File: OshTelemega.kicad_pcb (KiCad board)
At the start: 4 copper layers, 30 x 80 mm, 139 parts, among them J1 USB_C_Receptacle_USB2.0_16P, J10 SERVOS, J12 DEBUG, J2 Conn_02x04_Counter_Clockwise, J3 SMA_Edgelaunch, J4 USB_C_Receptacle_USB2.0_16P, J5 UFL, J6 RIGHT, J7 LEFT, J8 Conn_01x02, U1 STM32L151VCTx, U10 MMC5983MA, U11 TSM200N03, U12 LM293QT, U13 LM293QT, U14 TSM200N03, U15 LM293QT, U16 TSM200N03, U17 MCP73831-2-OT, U18 TC2185-3.3VxCTTR, U2 WE-TVS-82400102, U3 ADXL375, U4 MS5607-02BA, U5 MAX-M10S, U6 MCP130-xxxxTT, U7 W25Q64JVXGIQ, U8 CC1200, U9 BMI088, Y1 ABM8W-40.0000MHZ

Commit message: v0.1 done. Redesigning for potential mosaic integration
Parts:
- removed BZ1: Buzzer, Buzzer_Beeper:Buzzer_TDK_PS1240P02BT_D12.2mm_H6.5mm
- removed J1: USB_C_Receptacle_USB2.0_16P, Connector_USB:USB_C_Receptacle_GCT_USB4105-xx-A_16P_TopMnt_Horizontal
- removed U7: W25Q64JVXGIQ, FCU2025Lib:DFN_XGIQ TR_WIN
- added H5: MountingHole_Pad, MountingHole:MountingHole_3.2mm_M3_DIN965_Pad, F.Cu at (47.0, 65.5)
- added U19: W25Q64JVXGIQ, FCU2025Lib:DFN_XGIQ TR_WIN, B.Cu at (39.8, 39.9)
- moved J4 99.3 mm to (38.7, 96.7)
- moved R35 68.8 mm to (21.2, 80.1), turned to 90 degrees
- moved J10 68.7 mm to (36.4, 67.0), turned to 90 degrees
- moved R36 66.7 mm to (21.2, 78.2), turned to -90 degrees
- moved U16 65.7 mm to (23.5, 79.0), turned to -90 degrees
- moved R31 65.3 mm to (25.8, 80.1), turned to 90 degrees
- moved R33 64.2 mm to (21.2, 76.0), turned to 90 degrees
- moved R34 63.4 mm to (22.2, 76.0), turned to -90 degrees
- moved R32 63.0 mm to (25.8, 78.2), turned to -90 degrees
- moved R29 62.0 mm to (23.8, 76.0), turned to 90 degrees
- moved R30 61.2 mm to (24.8, 76.0), turned to -90 degrees
- moved U15 60.0 mm to (23.2, 73.8), turned to 0 degrees
- moved J2 53.9 mm to (30.3, 67.0), turned to 90 degrees
- moved R23 53.3 mm to (36.0, 76.6), turned to -90 degrees
- moved R24 51.6 mm to (36.0, 78.5), turned to 90 degrees
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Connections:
- J12 pad 2: /NRST -> /SWCLK
- J12 pad 4: /SWCLK -> /NRST
- J2 pad 3: /MOSI2 -> V_LIPO
- J2 pad 5: /CS_COMP1 -> /MOSI2
- J2 pad 6: /CS_COMP0 -> /CS_COMP1
- J2 pad 8: V_LIPO -> /CS_COMP0
- J4 pad A1: Net-(J4-GND-PadA1) -> GND
- J4 pad A12: Net-(J4-GND-PadA1) -> GND
- J4 pad A4: Net-(J4-VBUS-PadA4) -> VBUS
- J4 pad A5: unconnected-(J4-CC1-PadA5) -> Net-(J4-CC1)
- J4 pad A6: unconnected-(J4-D+-PadA6) -> Net-(J4-D+-PadA6)
- J4 pad A7: unconnected-(J4-D--PadA7) -> Net-(J4-D--PadA7)
- J4 pad A9: Net-(J4-VBUS-PadA4) -> VBUS
- J4 pad B1: Net-(J4-GND-PadA1) -> GND
- J4 pad B12: Net-(J4-GND-PadA1) -> GND
- J4 pad B4: Net-(J4-VBUS-PadA4) -> VBUS
- J4 pad B5: unconnected-(J4-CC2-PadB5) -> Net-(J4-CC2)
- J4 pad B6: unconnected-(J4-D+-PadB6) -> Net-(J4-D+-PadA6)
- J4 pad B7: unconnected-(J4-D--PadB7) -> Net-(J4-D--PadA7)
- J4 pad B9: Net-(J4-VBUS-PadA4) -> VBUS
- J4 pad S1: unconnected-(J4-SHIELD-PadS1) -> GND
- R1 pad 1: Net-(J1-CC1) -> Net-(J4-CC1)
- R10 pad 1: Net-(J1-D+-PadA6) -> Net-(J4-D+-PadA6)
- R2 pad 1: Net-(J1-CC2) -> Net-(J4-CC2)
- R21 pad 2: /FIRE_C -> /FIRE_D
- R22 pad 1: /FIRE_C -> /FIRE_D
- R22 pad 2: /GATE_C -> /GATE_D
- R23 pad 1: /FET_C -> /FET_D
- R23 pad 2: /SENSE_C -> /SENSE_D
- R24 pad 2: /SENSE_C -> /SENSE_D
- R25 pad 2: /FIRE_D -> /FIRE_C
- R26 pad 1: /FIRE_D -> /FIRE_C
- R26 pad 2: /GATE_D -> /GATE_C
- R27 pad 1: /FET_D -> /FET_C
- R27 pad 2: /SENSE_D -> /SENSE_C
- R28 pad 2: /SENSE_D -> /SENSE_C
- R6 pad 2: Net-(J10-Pin_3) -> Net-(J10-Pin_4)
- R7 pad 2: Net-(J10-Pin_4) -> Net-(J10-Pin_3)
- R9 pad 1: Net-(J1-D--PadA7) -> Net-(J4-D--PadA7)
- U14 pad 2: /GATE_D -> /GATE_C
- U14 pad 4: /GATE_C -> /GATE_D
- U14 pad 5_6: /FET_C -> /FET_D
- U14 pad 7_8: /FET_D -> /FET_C
- U15 pad 1: /GATE_E -> /GATE_F
- U15 pad 7: /GATE_F -> /GATE_E
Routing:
- net GND: track 58.8 -> 123.1 mm, vias 51 -> 109
- net /CMP_LDO_IN: track 5.13 -> 66.8 mm, vias 0 -> 5
- net V_LIPO: track 4.18 -> 61.6 mm
- net /SENSE_A: track 0.89 -> 57.1 mm, vias 0 -> 2
- net /CMP_RAIL: track 10.7 -> 66.9 mm, vias 2 -> 6
- net /SENSE_B: track 0.88 -> 56.5 mm, vias 0 -> 2
- net /V_PBATT: track 1.00 -> 52.4 mm, vias 0 -> 2
- net /V_BATT: track 1.00 -> 49.6 mm, vias 0 -> 2
- net /SENSE_F: track 0.87 -> 48.3 mm, vias 0 -> 4
- net /MISO2: track 9.17 -> 53.6 mm, vias 0 -> 2
- net /FIRE_B: track 1.00 -> 41.9 mm, vias 0 -> 2
- net /SENSE_C: track 0.89 -> 41.2 mm, vias 0 -> 6
- net /SCK2: track 4.25 -> 44.2 mm, vias 0 -> 2
- net /SENSE_D: track 0.88 -> 40.7 mm, vias 0 -> 2
- net /SENSE_E: track 0.89 -> 39.6 mm, vias 0 -> 4
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- added copper zone on B.Cu, net /FET_C
- added copper zone on B.Cu, net /FET_D
- added copper zone on B.Cu, net /FET_E
- added copper zone on B.Cu, net /FET_F
- added copper zone on In1.Cu, net V_PYRO
- removed copper zone on B.Cu, net VBUS
- removed copper zone on F.Cu, net V_PYRO

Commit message: before adding 10 pin companion
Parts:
- removed J12: DEBUG, Connector_PinHeader_1.27mm:PinHeader_2x02_P1.27mm_Vertical
- added J1: Conn_ARM_SWD_TagConnect_TC2030-NL, Connector:Tag-Connect_TC2030-IDC-NL_2x03_P1.27mm_Vertical, F.Cu at (48.0, 58.6)
- moved L6 0.68 mm to (37.1, 28.9), turned to 90 degrees
- moved C41 0.64 mm to (36.2, 28.9), turned to -90 degrees
- moved L1 0.52 mm to (42.6, 29.4)
- moved L8 0.14 mm to (35.3, 26.9)
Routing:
- net /NRST: track 110.3 -> 101.0 mm, vias 6 -> 4
- net /SWDIO: track 13.2 -> 8.94 mm, vias 0 -> 3
- net /SWCLK: track 10.1 -> 11.9 mm, vias 1 -> 3
- net /AC_MOSI1: track 19.8 -> 18.3 mm
- net /AC_MISO1: track 19.3 -> 17.9 mm
- net /AC_SCK1: track 23.8 -> 22.6 mm
- net Net-(C40-Pad1): track 3.47 -> 2.53 mm
- net GND: track 123.1 -> 123.8 mm, vias 109 -> 113
- net Net-(J3-In): track 3.71 -> 4.28 mm
- net +3V3: track 79.5 -> 79.8 mm, vias 34 -> 35

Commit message: v0.2 done - just needs review and silkscreens
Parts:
- removed FL1: B39162B4300F210, Filter:Filter_1411-5_1.4x1.1mm
- added C43: 10nF X7R, Capacitor_SMD:C_0402_1005Metric, B.Cu at (34.1, 35.5)
- added C44: 0.1uF, Capacitor_SMD:C_0402_1005Metric, B.Cu at (48.9, 71.2)
- added D2: BAT54CW, Package_TO_SOT_SMD:SOT-323_SC-70, B.Cu at (46.9, 74.7)
- added D5: LED_Dual_AAKK, LED_SMD:LED_LiteOn_LTST-C19HE1WT, F.Cu at (27.3, 65.4)
- added FB2: LQG15HS47NJ02, Inductor_SMD:L_0402_1005Metric, B.Cu at (33.2, 33.6)
- added J9: Conn_02x05_Counter_Clockwise, Connector_PinHeader_1.27mm:PinHeader_2x05_P1.27mm_Vertical, F.Cu at (37.2, 66.2)
- added Q1: SiA449DJ, Package_TO_SOT_SMD:Vishay_PowerPAK_SC70-6L_Single, B.Cu at (31.5, 87.4)
- added Q2: AO3400A, Package_TO_SOT_SMD:SOT-23, B.Cu at (31.5, 81.7)
- added Q3: SiA449DJ, Package_TO_SOT_SMD:Vishay_PowerPAK_SC70-6L_Single, B.Cu at (32.0, 84.7)
- added R49: 100k, Resistor_SMD:R_0402_1005Metric, B.Cu at (29.8, 88.0)
- added R50: 1k, Resistor_SMD:R_0402_1005Metric, B.Cu at (26.1, 64.7)
- added R51: 1k, Resistor_SMD:R_0402_1005Metric, B.Cu at (45.1, 69.2)
- added R52: 100k, Resistor_SMD:R_0402_1005Metric, B.Cu at (48.6, 74.0)
- added R53: 100k, Resistor_SMD:R_0402_1005Metric, B.Cu at (30.2, 85.1)
- added R54: 10R 0.25W, Resistor_SMD:R_0402_1005Metric, B.Cu at (33.2, 35.5)
- added U21: SN74LVC1G80QDCKTQ1, Package_TO_SOT_SMD:SOT-353_SC-70-5, B.Cu at (47.0, 71.3)
- added U7: DRV5012AEDMRR, Package_SON:Texas_X2SON-4-1EP_1.1x1.4mm_P0.5mm_EP0.8x0.6mm, F.Cu at (24.1, 66.0)
- C21: footprint Inductor_SMD:L_0402_1005Metric -> Capacitor_SMD:C_0402_1005Metric
- FB1: value FerriteBead -> LI0402C221R-10
- J1: value Conn_ARM_SWD_TagConnect_TC2030-NL -> TAGCONNECT
- J2: value Conn_02x04_Counter_Clockwise -> Conn_01x02; footprint Connector_PinHeader_1.27mm:PinHeader_2x04_P1.27mm_Vertical -> Connector_PinHeader_1.27mm:PinHeader_1x02_P1.27mm_Vertical
- J8: value Conn_01x02 -> BATT
- moved U6 13.5 mm to (47.8, 41.0), turned to 180 degrees
- moved C10 13.4 mm to (48.1, 43.2), turned to 0 degrees
- moved D1 13.2 mm to (34.8, 85.5), turned to 90 degrees
- moved J2 12.3 mm to (21.4, 58.6), turned to 0 degrees
- moved J5 10.7 mm to (35.4, 38.9), turned to 0 degrees
- moved C21 7.23 mm to (27.7, 94.6), turned to 0 degrees
- moved J10 5.26 mm to (31.2, 66.2)
- moved U19 2.73 mm to (42.4, 40.5)
- moved R40 2.43 mm to (25.3, 90.2)
- moved C23 2.41 mm to (23.7, 92.5)
- moved C24 2.41 mm to (22.8, 86.2)
- moved R41 2.41 mm to (25.3, 88.3)
- moved R42 2.41 mm to (24.3, 89.4)
- moved R43 2.41 mm to (24.3, 87.5)
- moved U18 2.41 mm to (22.1, 89.2)
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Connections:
- C23 pad 2: Net-(D1-K) -> V_LIPO
- D1 pad 1: Net-(D1-K) -> V_LIPO
- D1 pad 2: V_LIPO -> /MGSW_OUT
- J2 pad 1: GND -> /BUZZ
- J2 pad 2: /SCK2 -> GND
- J7 pad 8: V_CHARGE -> V_PROT
- R40 pad 2: Net-(D1-K) -> V_LIPO
- U1 pad 68: unconnected-(U1-PA9-Pad68) -> /TX1
- U1 pad 69: unconnected-(U1-PA10-Pad69) -> /RX1
- U18 pad 1: Net-(D1-K) -> V_LIPO
- U18 pad 3: Net-(D1-K) -> V_LIPO
- U5 pad 11: Net-(U5-RF_IN) -> Net-(J5-In)
- U5 pad 14: unconnected-(U5-VCC_RF-Pad14) -> Net-(U5-VCC_RF)
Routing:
- net /MGSW_IN: track 0.00 -> 93.4 mm, vias 0 -> 3
- net /HALL_OUT: track 0.00 -> 50.1 mm, vias 0 -> 6
- net /TX1: track 0.00 -> 30.8 mm, vias 0 -> 4
- net Net-(Q2-G): track 0.00 -> 27.4 mm, vias 0 -> 4
- net Net-(D5-A2): track 0.00 -> 24.8 mm, vias 0 -> 5
- net /NRST: track 101.0 -> 81.7 mm
- net /RX1: track 0.00 -> 17.4 mm, vias 0 -> 2
- net Net-(D1-K): track 12.1 -> 0.00 mm
- net /CS_COMP1: track 6.40 -> 17.7 mm
- net /CS_COMP0: track 6.72 -> 17.7 mm
- net /MOSI2: track 49.7 -> 40.7 mm, vias 3 -> 2
- net /SCK2: track 44.2 -> 52.6 mm, vias 2 -> 4
- net /CS_MAG: track 13.5 -> 21.0 mm, vias 0 -> 4
- net /BUZZ: track 0.00 -> 7.47 mm, vias 0 -> 2
- net V_PROT: track 0.00 -> 6.56 mm
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
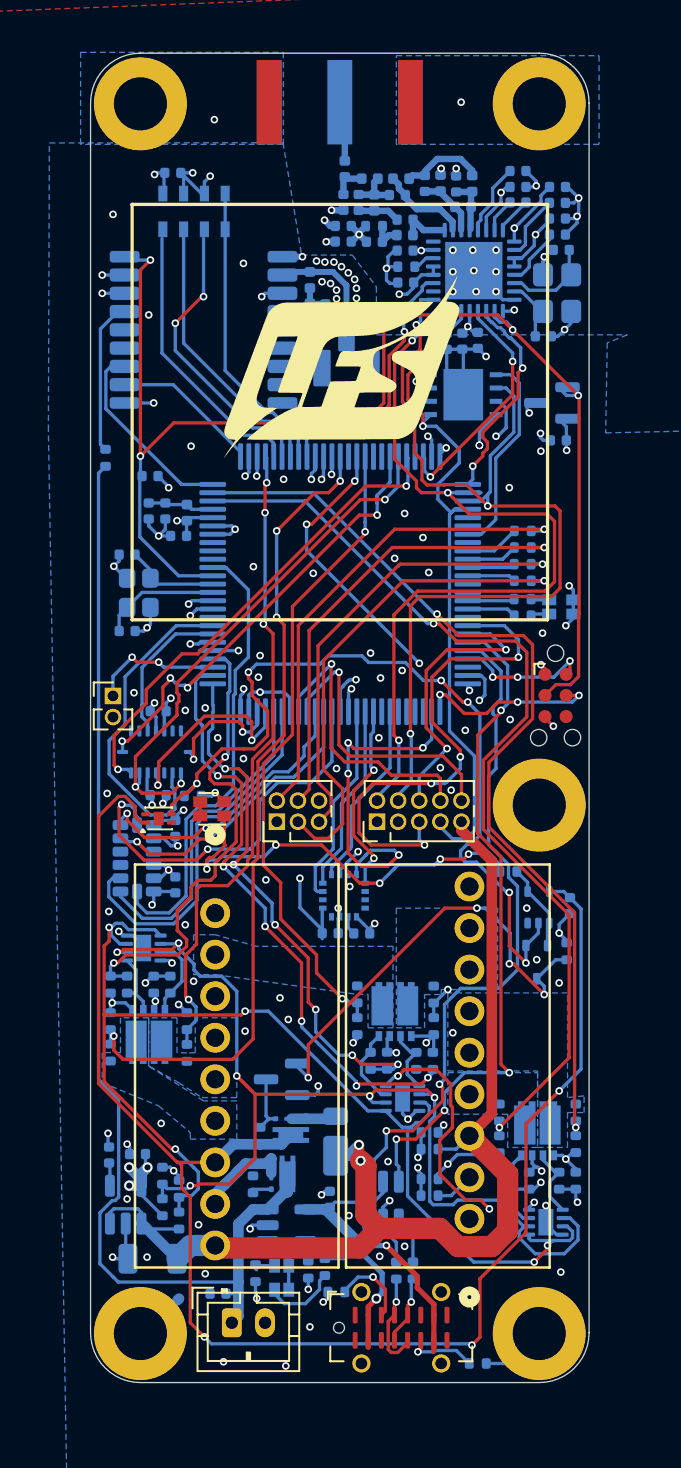
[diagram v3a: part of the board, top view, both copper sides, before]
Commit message: some jlc manufacturing considerations
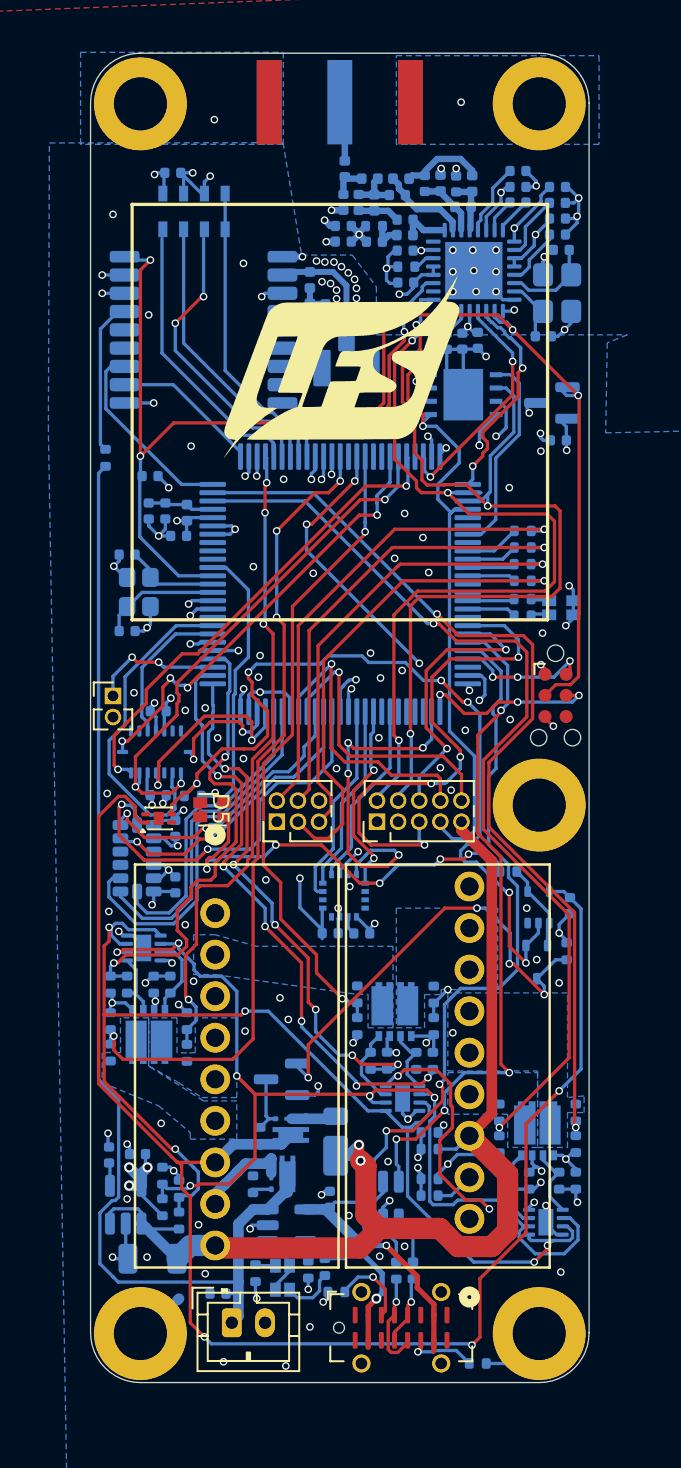
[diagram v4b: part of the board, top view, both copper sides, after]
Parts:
- removed ECS-160-8-36Q-AES-TR1: Crystal_GND24, Crystal:Crystal_SMD_2520-4Pin_2.5x2.0mm
- added X2: ECS-160-8-36Q-AES-TR, Crystal:Crystal_SMD_2520-4Pin_2.5x2.0mm, B.Cu at (22.9, 52.4)
- D3, D4, D5: footprint LED_SMD:LED_LiteOn_LTST-C19HE1WT -> FCU2025Lib:DualLED0606
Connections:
- D4 pad 3: Net-(D4-A2) -> Net-(D4-K1)
- D4 pad 4: Net-(D4-K2) -> Net-(D4-A1)
- R38 pad 2: Net-(D4-K2) -> Net-(D4-K1)
- R39 pad 1: Net-(D4-A1) -> Net-(D4-A2)
- U17 pad 1: Net-(D4-A2) -> Net-(D4-A1)
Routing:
- net Net-(D4-K1): track 0.00 -> 1.58 mm
- net Net-(D4-K2): track 1.17 -> 0.00 mm

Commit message: fixed wrong orientation on mag switch mosfet
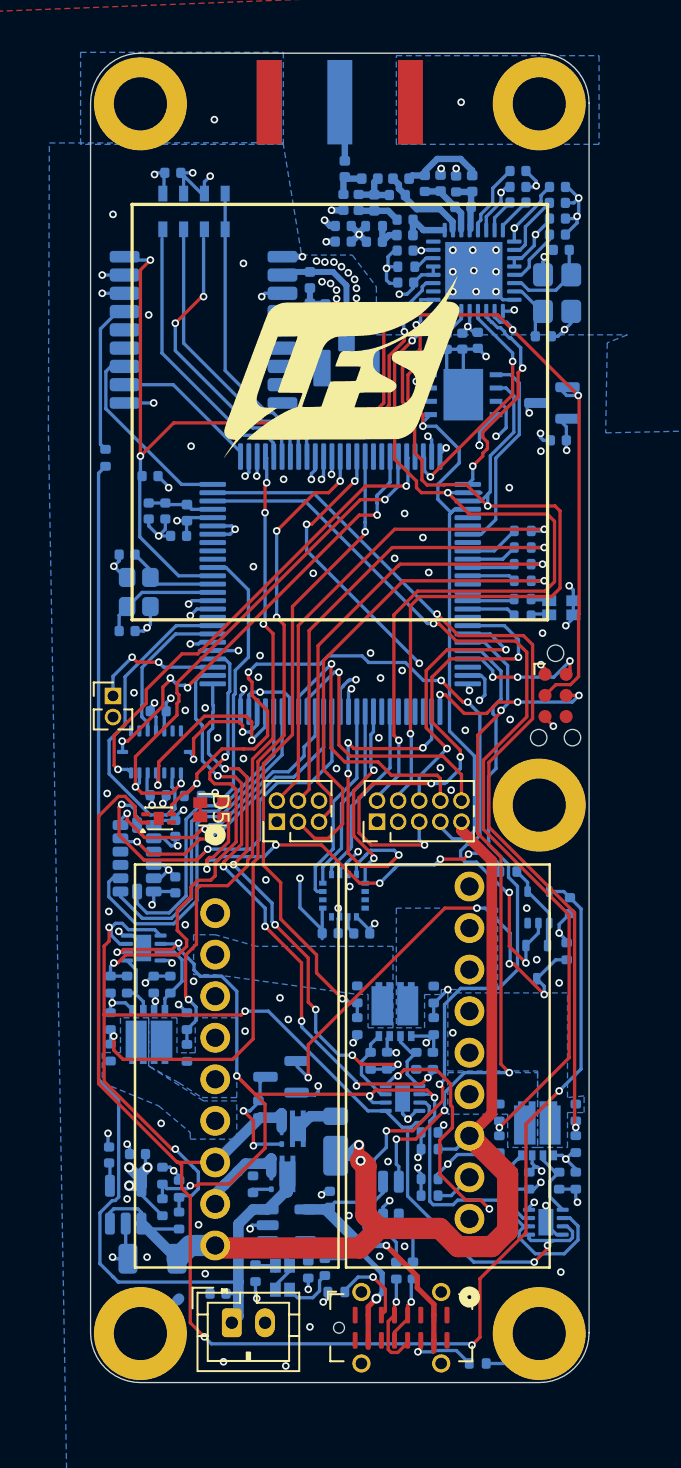
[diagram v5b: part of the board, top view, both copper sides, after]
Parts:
- X2: value ECS-160-8-36Q-AES-TR -> ECS-160-8-36Q-AES-TR1
- moved R53 1.60 mm to (30.1, 83.5)
- moved Q2 0.15 mm to (31.5, 81.5)
- moved Q3 0.11 mm to (32.1, 84.7), turned to 90 degrees
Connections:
- Q3 pad 1: /MGSW_IN -> /MGSW_OUT
- Q3 pad 4: /MGSW_OUT -> /MGSW_IN
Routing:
- net Net-(Q2-D): track 3.57 -> 6.92 mm, vias 0 -> 2
- net /MGSW_IN: track 93.4 -> 94.3 mm

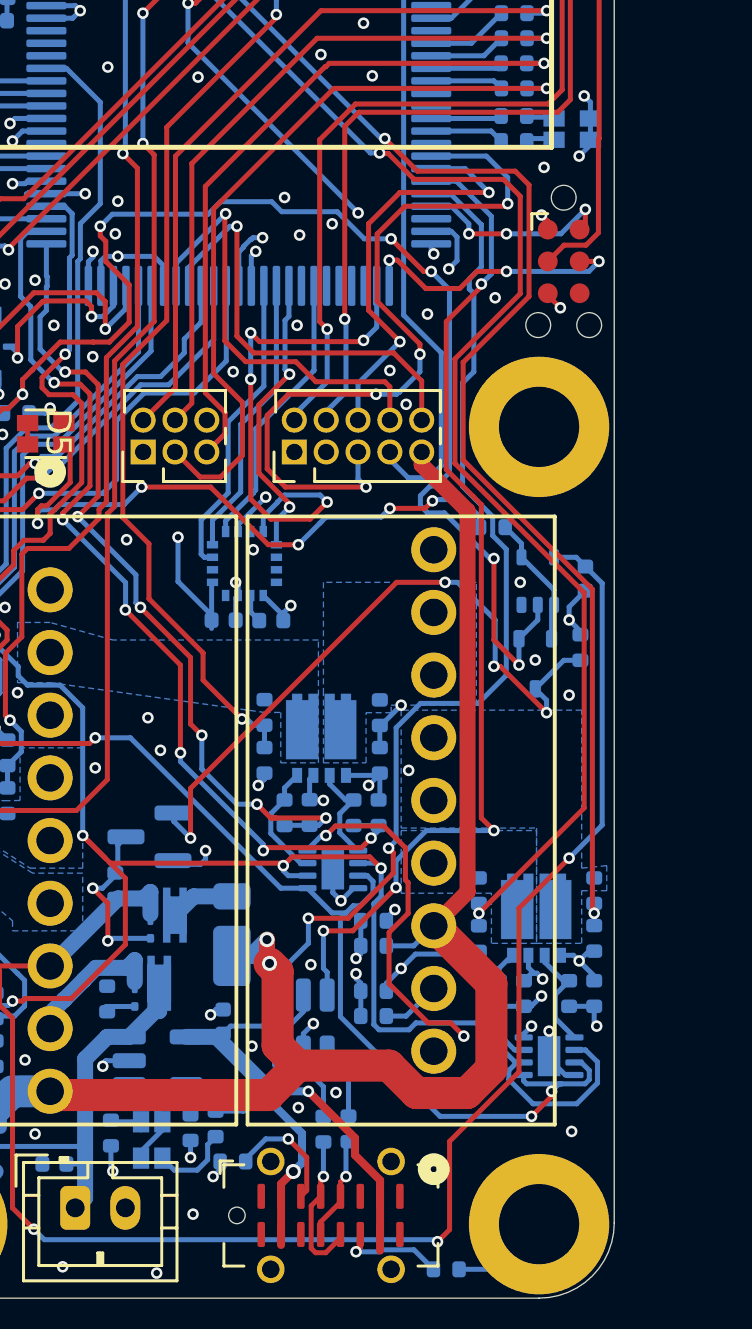
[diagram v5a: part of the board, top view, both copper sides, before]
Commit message: added pyro rp protection
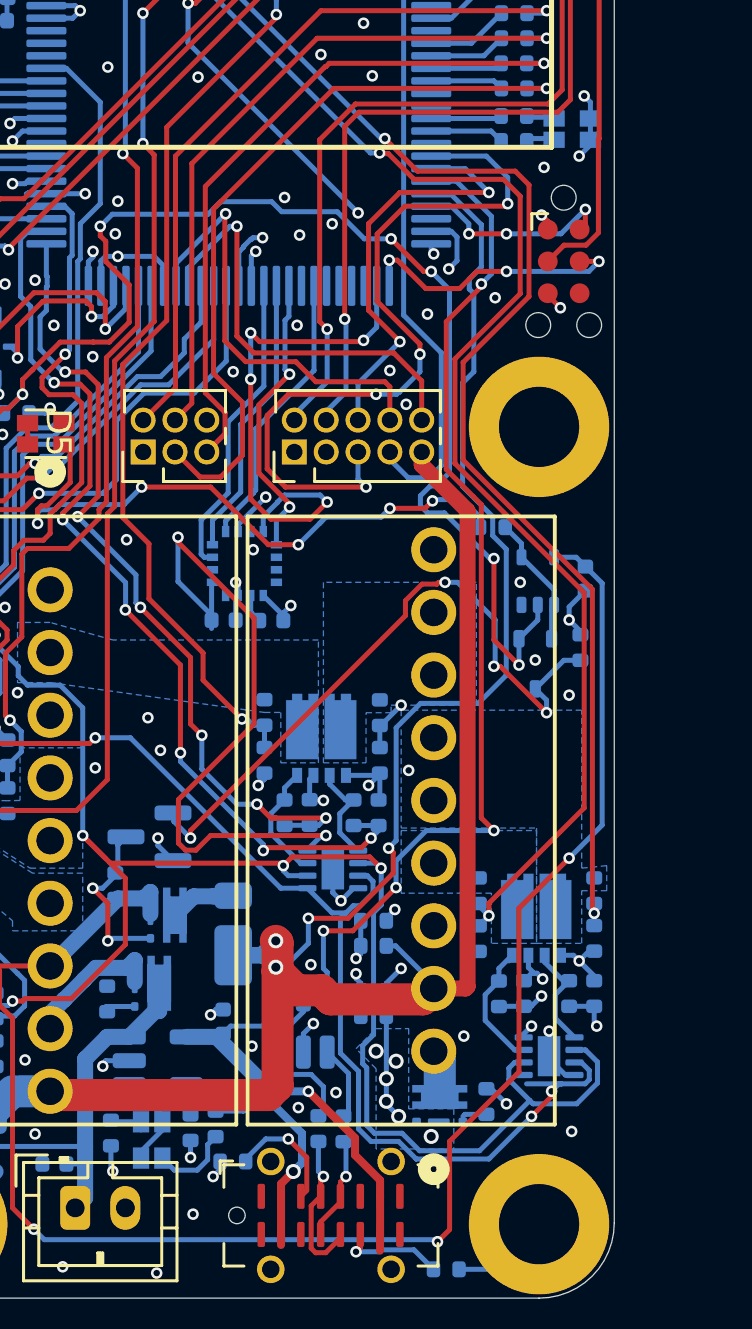
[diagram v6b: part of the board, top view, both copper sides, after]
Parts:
- added Q4: SiA449DJ, Package_TO_SOT_SMD:Vishay_PowerPAK_SC70-6L_Single, B.Cu at (43.0, 92.2)
- added R55: 100k, Resistor_SMD:R_0402_1005Metric, B.Cu at (44.9, 92.1)
- moved R10 0.20 mm to (38.2, 93.2)
- moved R9 0.20 mm to (39.2, 93.2)
- moved D1 0.06 mm to (34.8, 85.4)
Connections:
- J6 pad 1: GND -> Net-(J6-Pin_1)
- J6 pad 2: V_PYRO -> V_LIPO
- J6 pad 3: V_LIPO -> GND
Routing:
- net +3V3: track 82.4 -> 90.1 mm
- net V_LIPO: track 67.6 -> 62.3 mm
- net /CMP_RAIL: track 64.4 -> 69.7 mm
- net /CMP_LDO_IN: track 69.6 -> 72.8 mm
- net GND: track 126.5 -> 124.0 mm, vias 151 -> 152
- net V_PYRO: track 2.35 -> 4.20 mm, vias 0 -> 6
- net Net-(J6-Pin_1): track 0.00 -> 1.72 mm
- net Net-(R10-Pad2): track 3.69 -> 2.56 mm
- net Net-(Q4-G): track 0.00 -> 0.97 mm
- net Net-(Q2-G): track 27.4 -> 26.8 mm
- net /MGSW_OUT: track 2.80 -> 3.34 mm
- added copper zone on B.Cu, net V_PYRO
